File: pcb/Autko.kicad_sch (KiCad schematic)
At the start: 0 parts

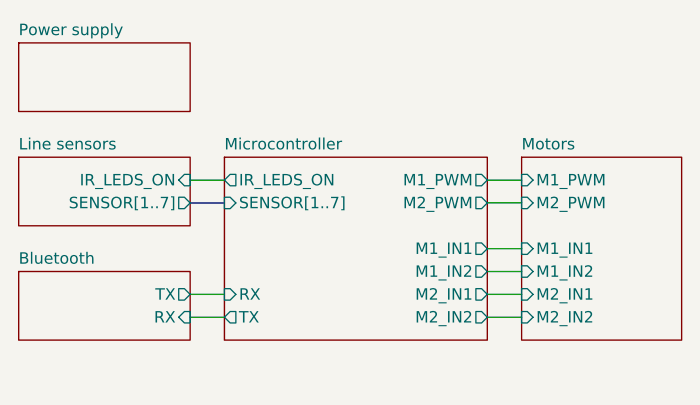
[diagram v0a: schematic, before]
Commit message: [pcb] Rework schematic for ATxmega16A4U
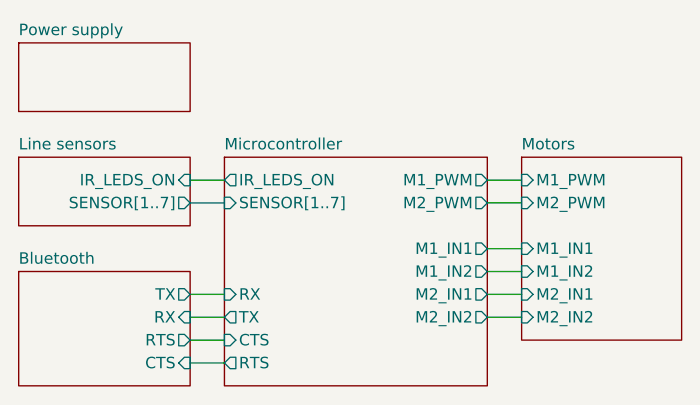
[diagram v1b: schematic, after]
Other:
- sheet Bluetooth ports: added CTS, RTS; removed none
- sheet Microcontroller ports: added CTS, RTS; removed none
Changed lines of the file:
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@@
+    (stroke (width 0) (type default))
+  )
+  (wire (pts (xy 43.18 60.96) (xy 46.99 60.96))
     (stroke (width 0) (type default))
   )
@@
   )
   (wire (pts (xy 43.18 40.64) (xy 46.99 40.64))
+    (stroke (width 0) (type default))
+  )
+  (wire (pts (xy 43.18 58.42) (xy 46.99 58.42))
     (stroke (width 0) (type default))
   )
@@
     )
   )
-  (sheet (at 24.13 50.8) (size 19.05 7.62) (fields_autoplaced)
+  (sheet (at 24.13 50.8) (size 19.05 12.7) (fields_autoplaced)
     (stroke (width 0.1524) (type solid))
     (fill (color 255 255 194 1.0000))
@@
       (effects (font (size 1.27 1.27)) (justify left bottom))
     )
-    (property "Sheetfile" "Bluetooth.kicad_sch" (at 24.13 59.0046 0)
+    (property "Sheetfile" "Bluetooth.kicad_sch" (at 24.13 64.0846 0)
       (effects (font (size 1.27 1.27)) (justify left top) hide)
     )
@@
       (effects (font (size 1.27 1.27)) (justify right))
     )
+    (pin "RTS" output (at 43.18 58.42 0)
+      (effects (font (size 1.27 1.27)) (justify right))
+    )
+    (pin "CTS" input (at 43.18 60.96 0)
+      (effects (font (size 1.27 1.27)) (justify right))
+    )
     (instances
       (project "Autko"
@@
     )
   )
-  (sheet (at 46.99 38.1) (size 29.21 20.32) (fields_autoplaced)
+  (sheet (at 46.99 38.1) (size 29.21 25.4) (fields_autoplaced)
     (stroke (width 0.1524) (type solid))
     (fill (color 255 255 194 1.0000))
@@
       (effects (font (size 1.27 1.27)) (justify left bottom))
     )
-    (property "Sheetfile" "Microcontroller.kicad_sch" (at 46.99 59.0046 0)
+    (property "Sheetfile" "Microcontroller.kicad_sch" (at 46.99 64.0846 0)
       (effects (font (size 1.27 1.27)) (justify left top) hide)
     )
@@
       (effects (font (size 1.27 1.27)) (justify left))
     )
+    (pin "RTS" output (at 46.99 60.96 180)
+      (effects (font (size 1.27 1.27)) (justify left))
+    )
+    (pin "CTS" input (at 46.99 58.42 180)
+      (effects (font (size 1.27 1.27)) (justify left))
+    )

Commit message: [pcb] 4 layer PCB
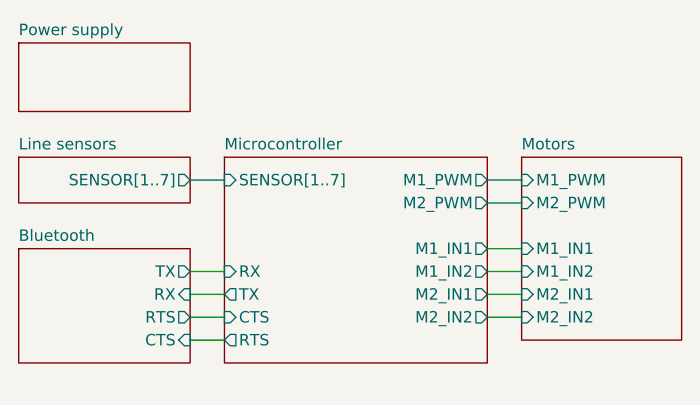
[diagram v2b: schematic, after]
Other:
- sheet Line sensors ports: added none; removed IR_LEDS_ON
- sheet Microcontroller ports: added none; removed IR_LEDS_ON
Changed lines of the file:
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@@
     (stroke (width 0) (type default))
   )
-  (wire (pts (xy 43.18 60.96) (xy 46.99 60.96))
+  (wire (pts (xy 43.18 50.8) (xy 46.99 50.8))
     (stroke (width 0) (type default))
   )
@@
   )
   (wire (pts (xy 76.2 50.8) (xy 80.01 50.8))
-    (stroke (width 0) (type default))
-  )
-  (wire (pts (xy 43.18 40.64) (xy 46.99 40.64))
     (stroke (width 0) (type default))
   )
@@
     (stroke (width 0) (type default))
   )
-  (bus (pts (xy 43.18 43.18) (xy 46.99 43.18))
+  (bus (pts (xy 43.18 40.64) (xy 46.99 40.64))
     (stroke (width 0) (type default))
   )
@@
     )
   )
-  (sheet (at 24.13 38.1) (size 19.05 7.62) (fields_autoplaced)
+  (sheet (at 24.13 38.1) (size 19.05 5.08) (fields_autoplaced)
     (stroke (width 0.1524) (type solid))
     (fill (color 255 255 194 1.0000))
@@
       (effects (font (size 1.27 1.27)) (justify left bottom))
     )
-    (property "Sheetfile" "Line_sensors.kicad_sch" (at 24.13 46.3046 0)
+    (property "Sheetfile" "Line_sensors.kicad_sch" (at 24.13 43.7646 0)
       (effects (font (size 1.27 1.27)) (justify left top) hide)
     )
-    (pin "IR_LEDS_ON" input (at 43.18 40.64 0)
-      (effects (font (size 1.27 1.27)) (justify right))
-    )
-    (pin "SENSOR[1..7]" output (at 43.18 43.18 0)
+    (pin "SENSOR[1..7]" output (at 43.18 40.64 0)
       (effects (font (size 1.27 1.27)) (justify right))
     )
@@
     )
   )
-  (sheet (at 24.13 50.8) (size 19.05 12.7) (fields_autoplaced)
+  (sheet (at 24.13 48.26) (size 19.05 12.7) (fields_autoplaced)
     (stroke (width 0.1524) (type solid))
     (fill (color 255 255 194 1.0000))
-    (property "Sheetname" "Bluetooth" (at 24.13 50.0884 0)
+    (property "Sheetname" "Bluetooth" (at 24.13 47.5484 0)
       (effects (font (size 1.27 1.27)) (justify left bottom))
     )
-    (property "Sheetfile" "Bluetooth.kicad_sch" (at 24.13 64.0846 0)
+    (property "Sheetfile" "Bluetooth.kicad_sch" (at 24.13 61.5446 0)
       (effects (font (size 1.27 1.27)) (justify left top) hide)
     )
-    (pin "TX" output (at 43.18 53.34 0)
+    (pin "TX" output (at 43.18 50.8 0)
       (effects (font (size 1.27 1.27)) (justify right))
     )
-    (pin "RX" input (at 43.18 55.88 0)
+    (pin "RX" input (at 43.18 53.34 0)
       (effects (font (size 1.27 1.27)) (justify right))
     )
-    (pin "RTS" output (at 43.18 58.42 0)
+    (pin "RTS" output (at 43.18 55.88 0)
       (effects (font (size 1.27 1.27)) (justify right))
     )
-    (pin "CTS" input (at 43.18 60.96 0)
+    (pin "CTS" input (at 43.18 58.42 0)
       (effects (font (size 1.27 1.27)) (justify right))
     )
@@
     )
   )
-  (sheet (at 46.99 38.1) (size 29.21 25.4) (fields_autoplaced)
+  (sheet (at 46.99 38.1) (size 29.21 22.86) (fields_autoplaced)
     (stroke (width 0.1524) (type solid))
     (fill (color 255 255 194 1.0000))
@@
       (effects (font (size 1.27 1.27)) (justify left bottom))
     )
-    (property "Sheetfile" "Microcontroller.kicad_sch" (at 46.99 64.0846 0)
+    (property "Sheetfile" "Microcontroller.kicad_sch" (at 46.99 61.5446 0)
       (effects (font (size 1.27 1.27)) (justify left top) hide)
     )
-    (pin "IR_LEDS_ON" output (at 46.99 40.64 180)
+    (pin "TX" output (at 46.99 53.34 180)
       (effects (font (size 1.27 1.27)) (justify left))
     )
-    (pin "TX" output (at 46.99 55.88 180)
-      (effects (font (size 1.27 1.27)) (justify left))
-    )
-    (pin "RX" input (at 46.99 53.34 180)
+    (pin "RX" input (at 46.99 50.8 180)
       (effects (font (size 1.27 1.27)) (justify left))
     )
@@
       (effects (font (size 1.27 1.27)) (justify right))
     )
-    (pin "SENSOR[1..7]" input (at 46.99 43.18 180)
+    (pin "SENSOR[1..7]" input (at 46.99 40.64 180)
       (effects (font (size 1.27 1.27)) (justify left))
     )
-    (pin "RTS" output (at 46.99 60.96 180)
+    (pin "RTS" output (at 46.99 58.42 180)
       (effects (font (size 1.27 1.27)) (justify left))
     )
-    (pin "CTS" input (at 46.99 58.42 180)
+    (pin "CTS" input (at 46.99 55.88 180)
       (effects (font (size 1.27 1.27)) (justify left))
     )

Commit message: [pcb] More final touches, UART test ponts added.
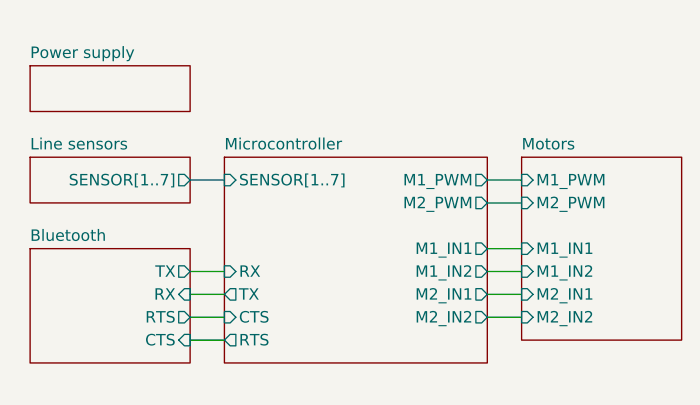
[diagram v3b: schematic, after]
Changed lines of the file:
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@@
     )
   )
-  (sheet (at 24.13 38.1) (size 19.05 5.08) (fields_autoplaced)
+  (sheet (at 25.4 38.1) (size 17.78 5.08) (fields_autoplaced)
     (stroke (width 0.1524) (type solid))
     (fill (color 255 255 194 1.0000))
-    (property "Sheetname" "Line sensors" (at 24.13 37.3884 0)
+    (property "Sheetname" "Line sensors" (at 25.4 37.3884 0)
       (effects (font (size 1.27 1.27)) (justify left bottom))
     )
-    (property "Sheetfile" "Line_sensors.kicad_sch" (at 24.13 43.7646 0)
+    (property "Sheetfile" "Line_sensors.kicad_sch" (at 25.4 43.7646 0)
       (effects (font (size 1.27 1.27)) (justify left top) hide)
     )
@@
     )
   )
-  (sheet (at 24.13 48.26) (size 19.05 12.7) (fields_autoplaced)
+  (sheet (at 25.4 48.26) (size 17.78 12.7) (fields_autoplaced)
     (stroke (width 0.1524) (type solid))
     (fill (color 255 255 194 1.0000))
-    (property "Sheetname" "Bluetooth" (at 24.13 47.5484 0)
+    (property "Sheetname" "Bluetooth" (at 25.4 47.5484 0)
       (effects (font (size 1.27 1.27)) (justify left bottom))
     )
-    (property "Sheetfile" "Bluetooth.kicad_sch" (at 24.13 61.5446 0)
+    (property "Sheetfile" "Bluetooth.kicad_sch" (at 25.4 61.5446 0)
       (effects (font (size 1.27 1.27)) (justify left top) hide)
     )
@@
     )
   )
-  (sheet (at 24.13 25.4) (size 19.05 7.62) (fields_autoplaced)
+  (sheet (at 25.4 27.94) (size 17.78 5.08) (fields_autoplaced)
     (stroke (width 0.1524) (type solid))
     (fill (color 255 255 194 1.0000))
-    (property "Sheetname" "Power supply" (at 24.13 24.6884 0)
+    (property "Sheetname" "Power supply" (at 25.4 27.2284 0)
       (effects (font (size 1.27 1.27)) (justify left bottom))
     )
-    (property "Sheetfile" "Power_supply.kicad_sch" (at 24.13 33.6046 0)
+    (property "Sheetfile" "Power_supply.kicad_sch" (at 25.4 33.6046 0)
       (effects (font (size 1.27 1.27)) (justify left top) hide)
     )

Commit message: [pcb] ERC/DRC checks
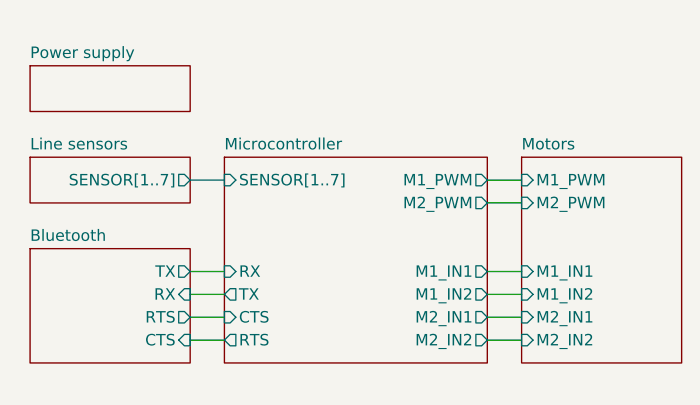
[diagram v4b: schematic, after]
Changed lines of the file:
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@@
 (kicad_sch (version 20230121) (generator eeschema)
   (paper "A4")
-  (wire (pts (xy 76.2 55.88) (xy 80.01 55.88))
+  (wire (pts (xy 76.2 58.42) (xy 80.01 58.42))
     (stroke (width 0) (type default))
   )
-  (wire (pts (xy 76.2 53.34) (xy 80.01 53.34))
+  (wire (pts (xy 76.2 55.88) (xy 80.01 55.88))
     (stroke (width 0) (type default))
   )
@@
     (stroke (width 0) (type default))
   )
-  (wire (pts (xy 76.2 50.8) (xy 80.01 50.8))
+  (wire (pts (xy 76.2 53.34) (xy 80.01 53.34))
     (stroke (width 0) (type default))
   )
@@
     (stroke (width 0) (type default))
   )
-  (wire (pts (xy 76.2 48.26) (xy 80.01 48.26))
+  (wire (pts (xy 76.2 50.8) (xy 80.01 50.8))
     (stroke (width 0) (type default))
   )
@@
     (stroke (width 0) (type default))
   )
-  (sheet (at 80.01 38.1) (size 17.78 20.32) (fields_autoplaced)
+  (sheet (at 80.01 38.1) (size 17.78 22.86) (fields_autoplaced)
     (stroke (width 0.1524) (type solid))
     (fill (color 255 255 194 1.0000))
@@
       (effects (font (size 1.27 1.27)) (justify left bottom))
     )
-    (property "Sheetfile" "Motors.kicad_sch" (at 80.01 59.0046 0)
+    (property "Sheetfile" "Motors.kicad_sch" (at 80.01 61.5446 0)
       (effects (font (size 1.27 1.27)) (justify left top) hide)
     )
@@
       (effects (font (size 1.27 1.27)) (justify left))
     )
-    (pin "M1_IN1" input (at 80.01 48.26 180)
+    (pin "M1_IN1" input (at 80.01 50.8 180)
       (effects (font (size 1.27 1.27)) (justify left))
     )
-    (pin "M2_IN1" input (at 80.01 53.34 180)
+    (pin "M2_IN1" input (at 80.01 55.88 180)
       (effects (font (size 1.27 1.27)) (justify left))
     )
-    (pin "M1_IN2" input (at 80.01 50.8 180)
+    (pin "M1_IN2" input (at 80.01 53.34 180)
       (effects (font (size 1.27 1.27)) (justify left))
     )
-    (pin "M2_IN2" input (at 80.01 55.88 180)
+    (pin "M2_IN2" input (at 80.01 58.42 180)
       (effects (font (size 1.27 1.27)) (justify left))
     )
@@
       (effects (font (size 1.27 1.27)) (justify right))
     )
-    (pin "M1_IN1" output (at 76.2 48.26 0)
+    (pin "M1_IN1" output (at 76.2 50.8 0)
       (effects (font (size 1.27 1.27)) (justify right))
     )
-    (pin "M2_IN1" output (at 76.2 53.34 0)
+    (pin "M2_IN1" output (at 76.2 55.88 0)
       (effects (font (size 1.27 1.27)) (justify right))
     )
-    (pin "M1_IN2" output (at 76.2 50.8 0)
+    (pin "M1_IN2" output (at 76.2 53.34 0)
       (effects (font (size 1.27 1.27)) (justify right))
     )
-    (pin "M2_IN2" output (at 76.2 55.88 0)
+    (pin "M2_IN2" output (at 76.2 58.42 0)
       (effects (font (size 1.27 1.27)) (justify right))
     )
